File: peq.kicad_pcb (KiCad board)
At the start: 2 copper layers, 55 x 95 mm, 79 parts, among them J5 DC_IN, J7 INPUT, J8 OUTPUT, Q1 2N3904, SW1 3PDT_FootSwitch, SW2 HIGH_FREQ_SW, SW3 LOW_FREQ_SW, SW4 SW_SPDT, U1 NJM4580

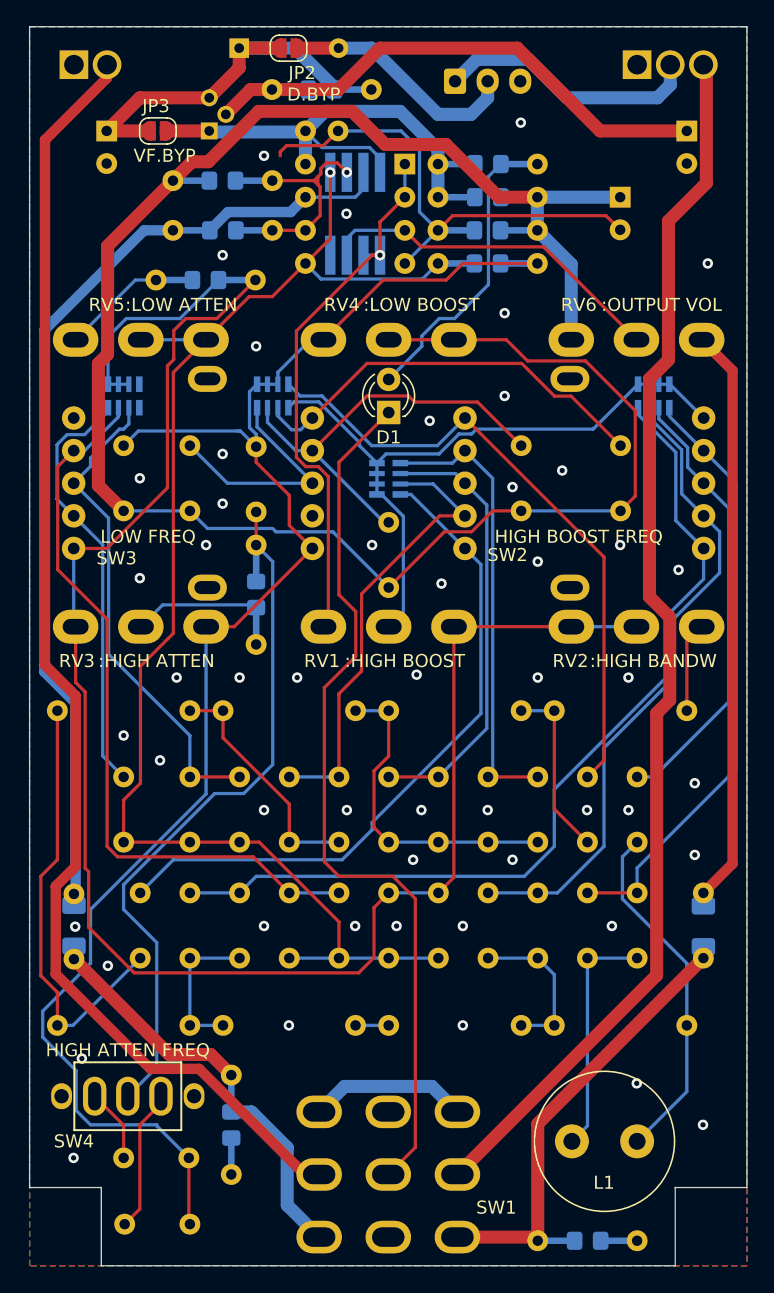
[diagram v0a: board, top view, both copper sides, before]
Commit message: add protection components and fix layout
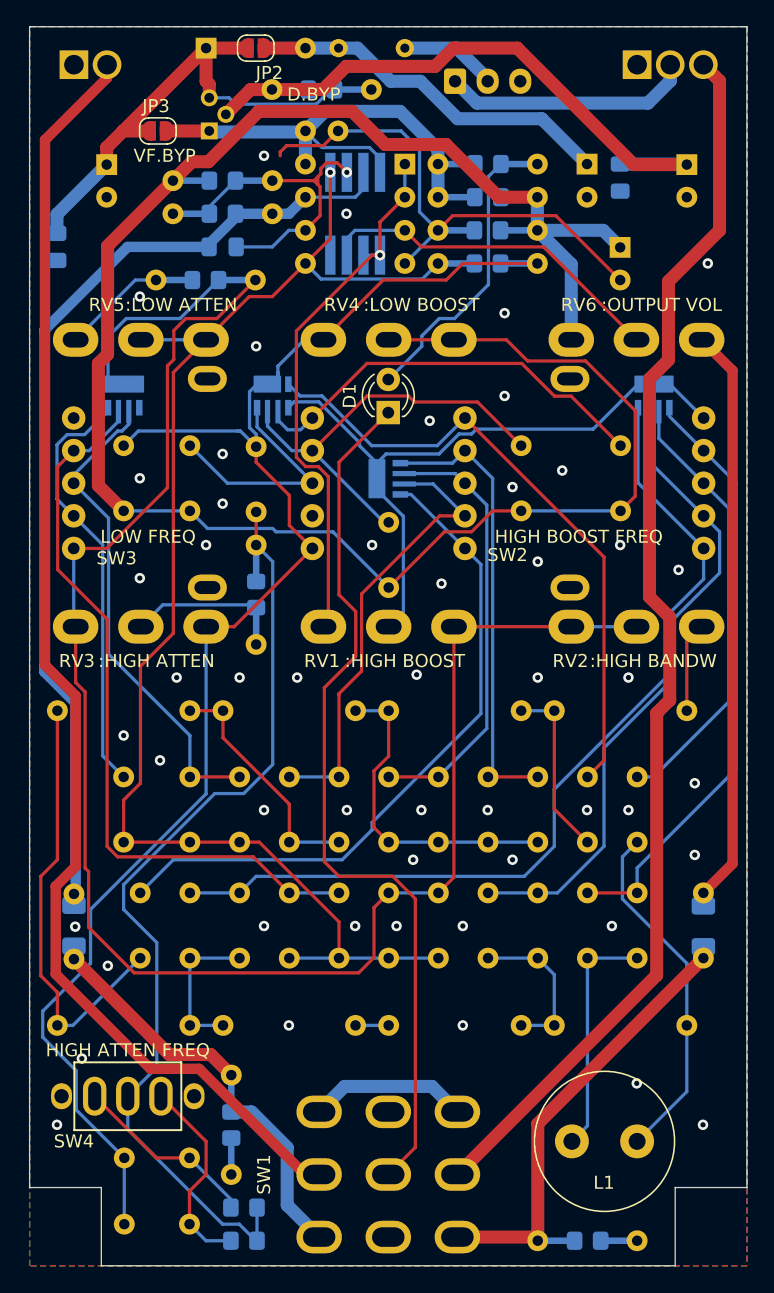
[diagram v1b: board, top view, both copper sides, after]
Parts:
- added C37: NC, Capacitor_SMD:C_0805_2012Metric_Pad1.18x1.45mm_HandSolder, B.Cu at (192.8, 73.9)
- added C38: 0.1u, Capacitor_SMD:C_0805_2012Metric_Pad1.18x1.45mm_HandSolder, B.Cu at (180.1, 73.9)
- added C39: 0.1u, Capacitor_SMD:C_0805_2012Metric_Pad1.18x1.45mm_HandSolder, B.Cu at (223.2, 68.6)
- added D3: D_Zener, Diode_THT:D_DO-35_SOD27_P2.54mm_Vertical_AnodeUp, B.Cu at (220.7, 67.5)
- added F1: Polyfuse, Resistor_THT:R_Axial_DIN0204_L3.6mm_D1.6mm_P5.08mm_Horizontal, B.Cu at (206.7, 58.6)
- added R10: 470k, Resistor_SMD:R_0805_2012Metric_Pad1.20x1.40mm_HandSolder, B.Cu at (194.4, 150.1)
- added R9: 470k, Resistor_SMD:R_0805_2012Metric_Pad1.20x1.40mm_HandSolder, B.Cu at (194.4, 147.5)
- D2: footprint Diode_THT:D_DO-34_SOD68_P7.62mm_Horizontal -> Diode_THT:D_DO-35_SOD27_P7.62mm_Horizontal
- R7: value 20k -> 47k
- RV2: value BANDWIDTH:B10k -> BANDWIDTH:B5k
- moved R7 7.73 mm to (189.0, 71.3), turned to 0 degrees
- moved C35 5.05 mm to (190.2, 143.7), turned to 180 degrees
- moved C36 4.97 mm to (190.2, 148.8), turned to 180 degrees
- moved C33 3.85 mm to (223.2, 73.9)
- moved C30 2.58 mm to (183.9, 67.6)
- moved C34 2.58 mm to (228.4, 67.6)
- moved D2 2.54 mm to (191.5, 58.6)
- moved JP2 2.51 mm to (195.3, 58.6)
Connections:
- J5 pad 2: Net-(D2-Pad2) -> Net-(J5-Pad2)
- RN1 pad 4: unconnected-(RN1-Pad4) -> LOW_ATTEN_BANK_IN
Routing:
- net Net-(C28-Pad1): track 53.3 -> 71.9 mm
- net Net-(D2-Pad2): track 18.5 -> 28.4 mm
- net Net-(Q1-Pad3): track 28.8 -> 38.3 mm
- net Net-(C35-Pad1): track 5.65 -> 14.4 mm
- net Net-(J5-Pad2): track 0.00 -> 7.50 mm
- net Net-(C37-Pad1): track 14.4 -> 21.1 mm
- net Net-(C34-Pad1): track 40.1 -> 46.3 mm
- net Net-(C36-Pad1): track 11.0 -> 15.5 mm
- net Net-(C31-Pad1): track 71.7 -> 74.9 mm
- net LOW_BOOST_BANK_IN: track 120.1 -> 116.9 mm
- net GND: track 37.5 -> 39.1 mm, vias 52 -> 51
- net GND_SWITCH: track 20.4 -> 19.1 mm
- net INPUT_JACK: track 94.4 -> 95.2 mm
- net LOW_ATTEN_BANK_IN: track 142.2 -> 143.0 mm
- net SW2C: track 34.2 -> 34.7 mm
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
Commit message: update comments and credits
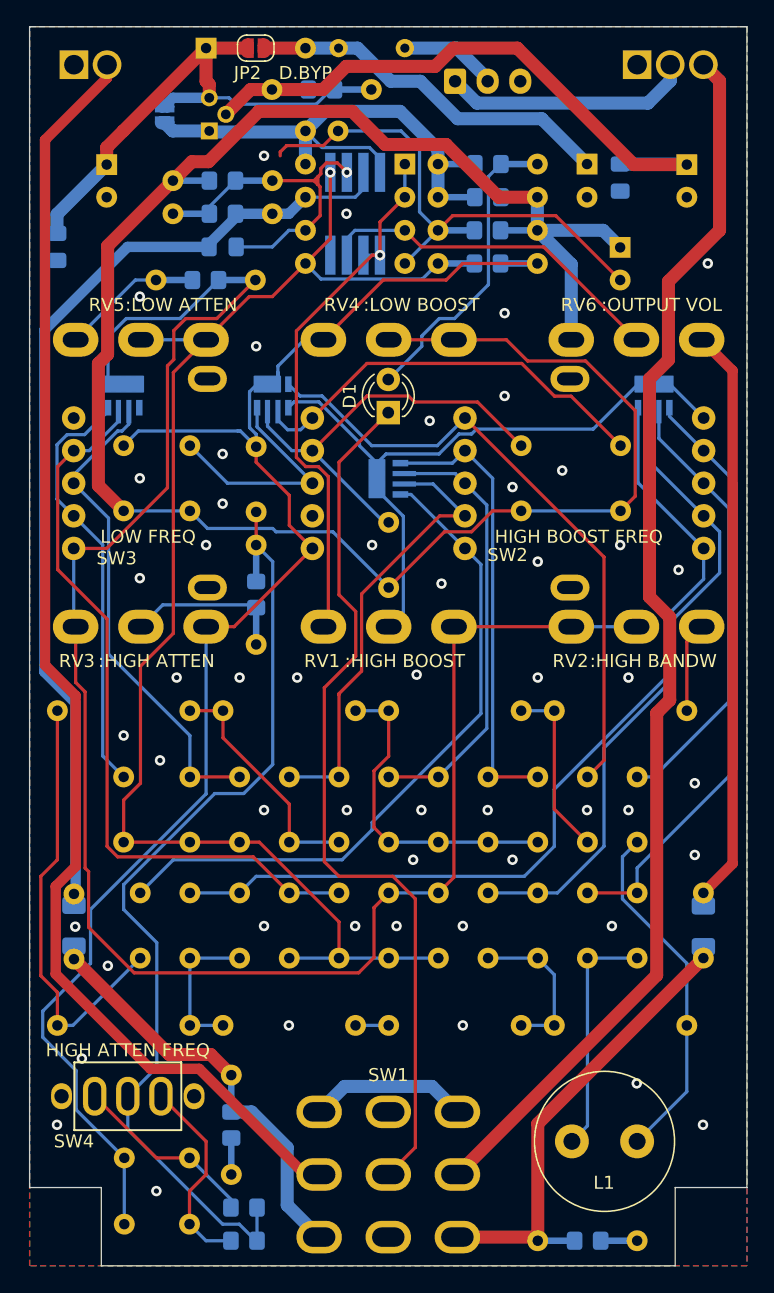
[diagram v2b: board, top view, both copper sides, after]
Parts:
- JP3: moved to B.Cu
- moved JP3 1.37 mm to (188.3, 63.7), turned to -90 degrees
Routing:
- net Net-(Q1-Pad3): track 38.3 -> 40.0 mm
- net GND: vias 51 -> 52
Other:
- board text added: "IN"
- board text added: "OUT"
- board text added: "PEQ rev.1.1 2024"
- board text added: "T | R | S"
- board text added: "T | S"
- board text removed: "INPUT"
- board text removed: "OUTPUT"
- board text removed: "PEQ rev.1.0 2024"
